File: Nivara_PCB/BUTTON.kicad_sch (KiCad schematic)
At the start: 4 parts, among them U12 LTV-357T

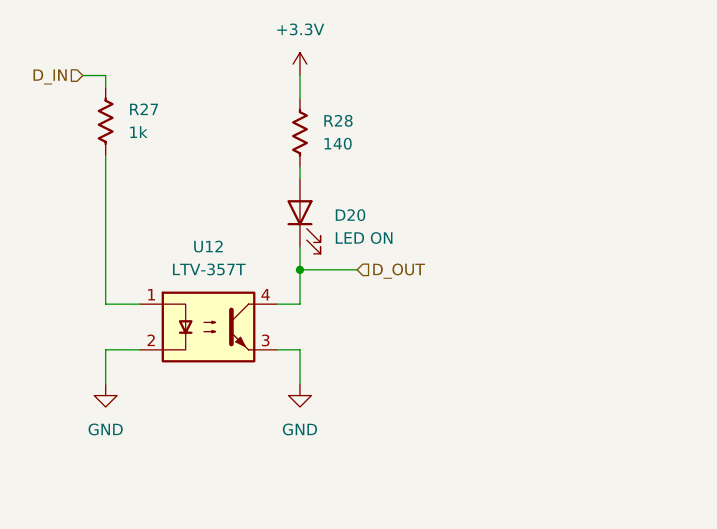
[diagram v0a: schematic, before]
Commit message: Cambios realizados en el PCB y el esquema de Nivara_PCB.
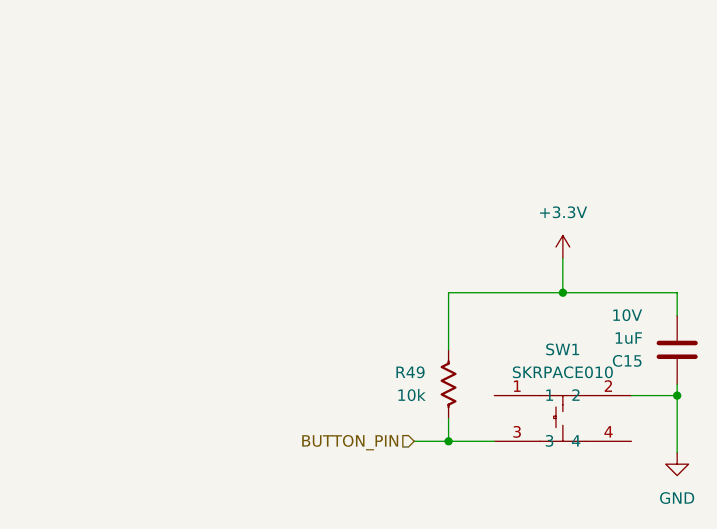
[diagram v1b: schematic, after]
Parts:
- removed D20: LED ON, LED_SMD:LED_0603_1608Metric, symbol Device:LED
- removed R27: 1k, PCM_Resistor_SMD_AKL:R_0603_1608Metric, symbol PCM_Resistor_US_AKL:R_0603
- removed R28: 140, PCM_Resistor_SMD_AKL:R_0603_1608Metric, symbol PCM_Resistor_US_AKL:R_0603
- removed U12: LTV-357T, Package_SO:SO-4_4.4x3.6mm_P2.54mm, symbol Isolator:LTV-357T
- added C15: 1uF, PCM_Capacitor_SMD_AKL:C_0603_1608Metric, symbol PCM_Capacitor_US_AKL:C_0603
- added R49: 10k, PCM_Resistor_SMD_AKL:R_0603_1608Metric, symbol PCM_Resistor_US_AKL:R_0603
- added SW1: SKRPACE010, EasyEDA:KEY-SMD_4P-L4.2-W3.2-P2.20-LS4.6, symbol EasyEDA:SKRPACE010
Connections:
- net +3.3V: now also C15.2, R49.1
- net GND: now also C15.1, SW1.2
- new net BUTTON_PIN: R49.2, SW1.3

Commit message: Cambios realizados en los archivos de Nivara_PCB.
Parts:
- C15: symbol PCM_Capacitor_US_AKL:C_0603 -> EasyEDA:C_0603
- R49: symbol PCM_Resistor_US_AKL:R_0603 -> EasyEDA:R_0603
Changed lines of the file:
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@@
 	)
 	(symbol
-		(lib_id "PCM_Resistor_US_AKL:R_0603")
+		(lib_id "EasyEDA:R_0603")
 		(at 92.71 81.28 0)
 		(mirror y)
@@
 	)
 	(symbol
-		(lib_id "power:GND")
+		(lib_id "EasyEDA:GND")
 		(at 118.11 88.9 0)
 		(unit 1)
@@
 	)
 	(symbol
-		(lib_id "power:+3.3V")
+		(lib_id "EasyEDA:+3.3V")
 		(at 105.41 67.31 0)
 		(mirror y)
@@
 	)
 	(symbol
-		(lib_id "PCM_Capacitor_US_AKL:C_0603")
+		(lib_id "EasyEDA:C_0603")
 		(at 118.11 77.47 180)
 		(unit 1)
